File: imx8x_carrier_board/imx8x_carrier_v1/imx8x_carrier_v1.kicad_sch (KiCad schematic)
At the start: 0 parts

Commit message: Schematic Updates
WIP
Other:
- note added: "JTAG-Misc..................................................Page 10"
- note removed: "GPIO-JTAG-Misc........................................Page 10"
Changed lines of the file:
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@@
 		)
 	)
-	(text "GPIO-JTAG-Misc........................................Page 10\n"
+	(text "JTAG-Misc..................................................Page 10\n"
 		(exclude_from_sim no)
 		(at 46.99 63.5 0)
@@
 			)
 		)
+		(property "Sim.Enable" "0"
+			(at 149.225 37.465 0)
+			(effects
+				(font
+					(size 1.27 1.27)
+				)
+				(hide yes)
+			)
+		)
 		(instances
 			(project "imx8x_carrier_v1"
@@
 			)
 		)
+		(property "Sim.Enable" "0"
+			(at 126.365 50.165 0)
+			(effects
+				(font
+					(size 1.27 1.27)
+				)
+				(hide yes)
+			)
+		)
 		(instances
 			(project "imx8x_carrier_v1"
@@
 			)
 		)
+		(property "Sim.Enable" "0"
+			(at 126.365 45.72 0)
+			(effects
+				(font
+					(size 1.27 1.27)
+				)
+				(hide yes)
+			)
+		)
 		(instances
 			(project "imx8x_carrier_v1"
@@
 			)
 		)
+		(property "Sim.Enable" "0"
+			(at 149.225 59.69 0)
+			(effects
+				(font
+					(size 1.27 1.27)
+				)
+				(hide yes)
+			)
+		)
 		(instances
 			(project "imx8x_carrier_v1"
@@
 			)
 		)
+		(property "Sim.Enable" "0"
+			(at 160.655 33.02 0)
+			(effects
+				(font
+					(size 1.27 1.27)
+				)
+				(hide yes)
+			)
+		)
 		(instances
 			(project "imx8x_carrier_v1"
@@
 			)
 		)
+		(property "Sim.Enable" "0"
+			(at 160.655 85.725 0)
+			(effects
+				(font
+					(size 1.27 1.27)
+				)
+				(hide yes)
+			)
+		)
 		(instances
 			(project "imx8x_carrier_v1"
@@
 			)
 		)
+		(property "Sim.Enable" "0"
+			(at 173.355 58.42 0)
+			(effects
+				(font
+					(size 1.27 1.27)
+				)
+				(hide yes)
+			)
+		)
 		(instances
 			(project "imx8x_carrier_v1"
@@
 			)
 		)
+		(property "Sim.Enable" "0"
+			(at 119.38 89.535 0)
+			(effects
+				(font
+					(size 1.27 1.27)
+				)
+				(hide yes)
+			)
+		)
 		(instances
 			(project ""
@@
 			)
 		)
+		(property "Sim.Enable" "0"
+			(at 137.795 27.305 0)
+			(effects
+				(font
+					(size 1.27 1.27)
+				)
+				(hide yes)
+			)
+		)
 		(instances
 			(project "imx8x_carrier_v1"
@@
 			)
 		)
+		(property "Sim.Enable" "0"
+			(at 149.225 67.945 0)
+			(effects
+				(font
+					(size 1.27 1.27)
+				)
+				(hide yes)
+			)
+		)
 		(instances
 			(project "imx8x_carrier_v1"
@@
 			)
 		)
+		(property "Sim.Enable" "0"
+			(at 149.225 48.26 0)
+			(effects
+				(font
+					(size 1.27 1.27)
+				)
+				(hide yes)
+			)
+		)
 		(instances
 			(project "imx8x_carrier_v1"
@@
 			(at 149.225 78.74 0)
 			(effects
+				(font
+					(size 1.27 1.27)
+				)
+				(hide yes)
+			)
+		)
+		(property "Sim.Enable" "0"
+			(at 149.225 78.74 0)
+			(effects

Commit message: Schematic Updates
WIP
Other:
- sheet GPIO - JTAG - Misc. renamed JTAG - Misc. (page 10)

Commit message: Update to Schematic
Did some overview of the schematic and did some touch ups. There are still some GPIOs that need to wired to pins.
All signals should be named correctly and connected the same.

Will need a document review before PCB layout.
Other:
- note added: "Need to put in all the GPIO remaining pins"
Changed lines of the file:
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@@
+		)
+	)
+	(text "Need to put in all the GPIO remaining pins"
+		(exclude_from_sim no)
+		(at 40.64 85.725 0)
+		(effects
+			(font
+				(size 1.27 1.27)
+			)
 		)
 	)
@@
 		(at 147.955 41.91 0)
 		(unit 1)
-		(exclude_from_sim yes)
+		(exclude_from_sim no)
 		(in_bom no)
 		(on_board no)
@@
 		(at 125.095 54.61 0)
 		(unit 1)
-		(exclude_from_sim yes)
+		(exclude_from_sim no)
 		(in_bom no)
 		(on_board no)
@@
 		(at 125.095 50.165 0)
 		(unit 1)
-		(exclude_from_sim yes)
+		(exclude_from_sim no)
 		(in_bom no)
 		(on_board no)
@@
 		(at 147.955 64.135 0)
 		(unit 1)
-		(exclude_from_sim yes)
+		(exclude_from_sim no)
 		(in_bom no)
 		(on_board no)
@@
 		(at 159.385 37.465 270)
 		(unit 1)
-		(exclude_from_sim yes)
+		(exclude_from_sim no)
 		(in_bom no)
 		(on_board no)
@@
 		(at 159.385 90.17 90)
 		(unit 1)
-		(exclude_from_sim yes)
+		(exclude_from_sim no)
 		(in_bom no)
 		(on_board no)
@@
 		(at 172.085 62.865 0)
 		(unit 1)
-		(exclude_from_sim yes)
+		(exclude_from_sim no)
 		(in_bom no)
 		(on_board no)
@@
 		(at 118.11 93.98 0)
 		(unit 1)
-		(exclude_from_sim yes)
+		(exclude_from_sim no)
 		(in_bom no)
 		(on_board no)
@@
 		(at 136.525 31.75 0)
 		(unit 1)
-		(exclude_from_sim yes)
+		(exclude_from_sim no)
 		(in_bom no)
 		(on_board no)
@@
 		(at 147.955 72.39 0)
 		(unit 1)
-		(exclude_from_sim yes)
+		(exclude_from_sim no)
 		(in_bom no)
 		(on_board no)
@@
 		(at 147.955 52.705 0)
 		(unit 1)
-		(exclude_from_sim yes)
+		(exclude_from_sim no)
 		(in_bom no)
 		(on_board no)
@@
 		(at 147.955 83.185 0)
 		(unit 1)
-		(exclude_from_sim yes)
-		(in_bom no)
-		(on_board no)
+		(exclude_from_sim no)
+		(in_bom no)
+		(on_board no)

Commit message: WIP
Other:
- sheet JTAG - Misc. (page 10) renamed JTAG - Misc.
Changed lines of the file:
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@@
 			(color 255 223 38 1.0000)
 		)
-		(property "Sheetname" "JTAG - Misc. (page 10)"
+		(property "Sheetname" "JTAG - Misc."
 			(at 127.635 80.5684 0)
 			(effects

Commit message: Schematic Complete
The IMX8X Scales carrier board is done being finalized. Cleaned up lots of things. This updated schematic should be ready for a full layout and track routing process. Only ERC errors are pin types which we dont really care about. All capacitor voltages have been reincluded since they were cleared by a kicad bug.
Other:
- note removed: "Need to put in all the GPIO remaining pins"
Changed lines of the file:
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@@
-		)
-	)
-	(text "Need to put in all the GPIO remaining pins"
-		(exclude_from_sim no)
-		(at 40.64 85.725 0)
-		(effects
-			(font
-				(size 1.27 1.27)
-			)
 		)
 	)
@@
 	)
 	(symbol
-		(lib_id "Graphic:SYM_Arrow_Normal")
+		(lib_id "imx8_carrier_board_symbol_library:SYM_Arrow_Normal")
 		(at 147.955 41.91 0)
 		(unit 1)
 		(exclude_from_sim no)
 		(in_bom no)
-		(on_board no)
+		(on_board yes)
 		(dnp no)
 		(fields_autoplaced yes)
@@
 		)
 		(property "Description" "Filled arrow, 200mil"
+			(at 147.955 41.91 0)
+			(effects
+				(font
+					(size 1.27 1.27)
+				)
+				(hide yes)
+			)
+		)
+		(property "Sim.Enable" "0"
 			(at 147.955 41.91 0)
 			(effects
@@
 	)
 	(symbol
-		(lib_id "Graphic:SYM_Arrow_Normal")
+		(lib_id "imx8_carrier_board_symbol_library:SYM_Arrow_Normal")
 		(at 125.095 54.61 0)
 		(unit 1)
 		(exclude_from_sim no)
 		(in_bom no)
-		(on_board no)
+		(on_board yes)
 		(dnp no)
 		(fields_autoplaced yes)
@@
 		)
 		(property "Description" "Filled arrow, 200mil"
+			(at 125.095 54.61 0)
+			(effects
+				(font
+					(size 1.27 1.27)
+				)
+				(hide yes)
+			)
+		)
+		(property "Sim.Enable" "0"
 			(at 125.095 54.61 0)
 			(effects
@@
 	)
 	(symbol
-		(lib_id "Graphic:SYM_Arrow_Normal")
+		(lib_id "imx8_carrier_board_symbol_library:SYM_Arrow_Normal")
 		(at 125.095 50.165 0)
 		(unit 1)
 		(exclude_from_sim no)
 		(in_bom no)
-		(on_board no)
+		(on_board yes)
 		(dnp no)
 		(fields_autoplaced yes)
@@
 		)
 		(property "Description" "Filled arrow, 200mil"
+			(at 125.095 50.165 0)
+			(effects
+				(font
+					(size 1.27 1.27)
+				)
+				(hide yes)
+			)
+		)
+		(property "Sim.Enable" "0"
 			(at 125.095 50.165 0)
 			(effects
@@
 	)
 	(symbol
-		(lib_id "Graphic:SYM_Arrow_Normal")
+		(lib_id "imx8_carrier_board_symbol_library:SYM_Arrow_Normal")
 		(at 147.955 64.135 0)
 		(unit 1)
 		(exclude_from_sim no)
 		(in_bom no)
-		(on_board no)
+		(on_board yes)
 		(dnp no)
 		(fields_autoplaced yes)
@@
 		)
 		(property "Description" "Filled arrow, 200mil"
+			(at 147.955 64.135 0)
+			(effects
+				(font
+					(size 1.27 1.27)
+				)
+				(hide yes)
+			)
+		)
+		(property "Sim.Enable" "0"
 			(at 147.955 64.135 0)
 			(effects
@@
 	)
 	(symbol
-		(lib_id "Graphic:SYM_Arrow_Normal")
+		(lib_id "imx8_carrier_board_symbol_library:SYM_Arrow_Normal")
 		(at 159.385 37.465 270)
 		(unit 1)
 		(exclude_from_sim no)
 		(in_bom no)
-		(on_board no)
+		(on_board yes)
 		(dnp no)
 		(fields_autoplaced yes)
@@
 		)
 		(property "Description" "Filled arrow, 200mil"
+			(at 159.385 37.465 0)
+			(effects
+				(font
+					(size 1.27 1.27)
+				)
+				(hide yes)
+			)
+		)
+		(property "Sim.Enable" "0"
 			(at 159.385 37.465 0)
 			(effects
@@
 	)
 	(symbol
-		(lib_id "Graphic:SYM_Arrow_Normal")
+		(lib_id "imx8_carrier_board_symbol_library:SYM_Arrow_Normal")
 		(at 159.385 90.17 90)
 		(unit 1)
 		(exclude_from_sim no)
 		(in_bom no)
-		(on_board no)
+		(on_board yes)
 		(dnp no)
 		(fields_autoplaced yes)
@@
 		)
 		(property "Description" "Filled arrow, 200mil"
+			(at 159.385 90.17 0)
+			(effects
+				(font
+					(size 1.27 1.27)
+				)
+				(hide yes)
+			)
+		)
+		(property "Sim.Enable" "0"
 			(at 159.385 90.17 0)
 			(effects
@@
 	)
 	(symbol
-		(lib_id "Graphic:SYM_Arrow_Normal")
+		(lib_id "imx8_carrier_board_symbol_library:SYM_Arrow_Normal")
 		(at 172.085 62.865 0)
 		(unit 1)
 		(exclude_from_sim no)
 		(in_bom no)
-		(on_board no)
+		(on_board yes)
 		(dnp no)
 		(fields_autoplaced yes)
@@
 		)
 		(property "Description" "Filled arrow, 200mil"
+			(at 172.085 62.865 0)
+			(effects
+				(font
+					(size 1.27 1.27)
+				)
+				(hide yes)
+			)
+		)
+		(property "Sim.Enable" "0"
 			(at 172.085 62.865 0)
 			(effects
@@
 	)
 	(symbol
-		(lib_id "Graphic:SYM_Arrow_Normal")
+		(lib_id "imx8_carrier_board_symbol_library:SYM_Arrow_Normal")
 		(at 118.11 93.98 0)
 		(unit 1)
 		(exclude_from_sim no)
 		(in_bom no)
-		(on_board no)
+		(on_board yes)
 		(dnp no)
 		(fields_autoplaced yes)
@@
 		)
 		(property "Description" "Filled arrow, 200mil"
+			(at 118.11 93.98 0)
+			(effects
+				(font
+					(size 1.27 1.27)
+				)
+				(hide yes)
+			)
+		)
+		(property "Sim.Enable" "0"
 			(at 118.11 93.98 0)
 			(effects
@@
 	)
 	(symbol
-		(lib_id "Graphic:SYM_Arrow_Normal")
+		(lib_id "imx8_carrier_board_symbol_library:SYM_Arrow_Normal")
 		(at 136.525 31.75 0)
 		(unit 1)
 		(exclude_from_sim no)
 		(in_bom no)
-		(on_board no)
+		(on_board yes)
 		(dnp no)
 		(fields_autoplaced yes)
@@
 		)
 		(property "Description" "Filled arrow, 200mil"
+			(at 136.525 31.75 0)
+			(effects
+				(font
+					(size 1.27 1.27)
+				)
+				(hide yes)
+			)
+		)
+		(property "Sim.Enable" "0"
 			(at 136.525 31.75 0)
 			(effects
@@
 	)
 	(symbol
-		(lib_id "Graphic:SYM_Arrow_Normal")
+		(lib_id "imx8_carrier_board_symbol_library:SYM_Arrow_Normal")
 		(at 147.955 72.39 0)
 		(unit 1)
 		(exclude_from_sim no)
 		(in_bom no)
-		(on_board no)
+		(on_board yes)
 		(dnp no)
 		(fields_autoplaced yes)
@@
 		)
 		(property "Description" "Filled arrow, 200mil"
+			(at 147.955 72.39 0)
+			(effects
+				(font
+					(size 1.27 1.27)
+				)
+				(hide yes)
+			)
+		)
+		(property "Sim.Enable" "0"
 			(at 147.955 72.39 0)
 			(effects
@@
 	)
 	(symbol
-		(lib_id "Graphic:SYM_Arrow_Normal")
+		(lib_id "imx8_carrier_board_symbol_library:SYM_Arrow_Normal")
 		(at 147.955 52.705 0)
 		(unit 1)
 		(exclude_from_sim no)
 		(in_bom no)
-		(on_board no)
+		(on_board yes)
 		(dnp no)
 		(fields_autoplaced yes)
@@
 		)
 		(property "Description" "Filled arrow, 200mil"
+			(at 147.955 52.705 0)
+			(effects
+				(font
+					(size 1.27 1.27)
+				)
+				(hide yes)
+			)
+		)
+		(property "Sim.Enable" "0"
 			(at 147.955 52.705 0)
 			(effects
@@
 	)
 	(symbol
-		(lib_id "Graphic:SYM_Arrow_Normal")
+		(lib_id "imx8_carrier_board_symbol_library:SYM_Arrow_Normal")
 		(at 147.955 83.185 0)
 		(unit 1)
 		(exclude_from_sim no)
 		(in_bom no)
-		(on_board no)
+		(on_board yes)
 		(dnp no)
 		(fields_autoplaced yes)
@@
 			(at 147.955 83.185 0)
 			(effects
+				(font
+					(size 1.27 1.27)
+				)
+				(hide yes)
+			)
+		)
+		(property "Sim.Enable" "0"
+			(at 147.955 83.185 0)
+			(effects

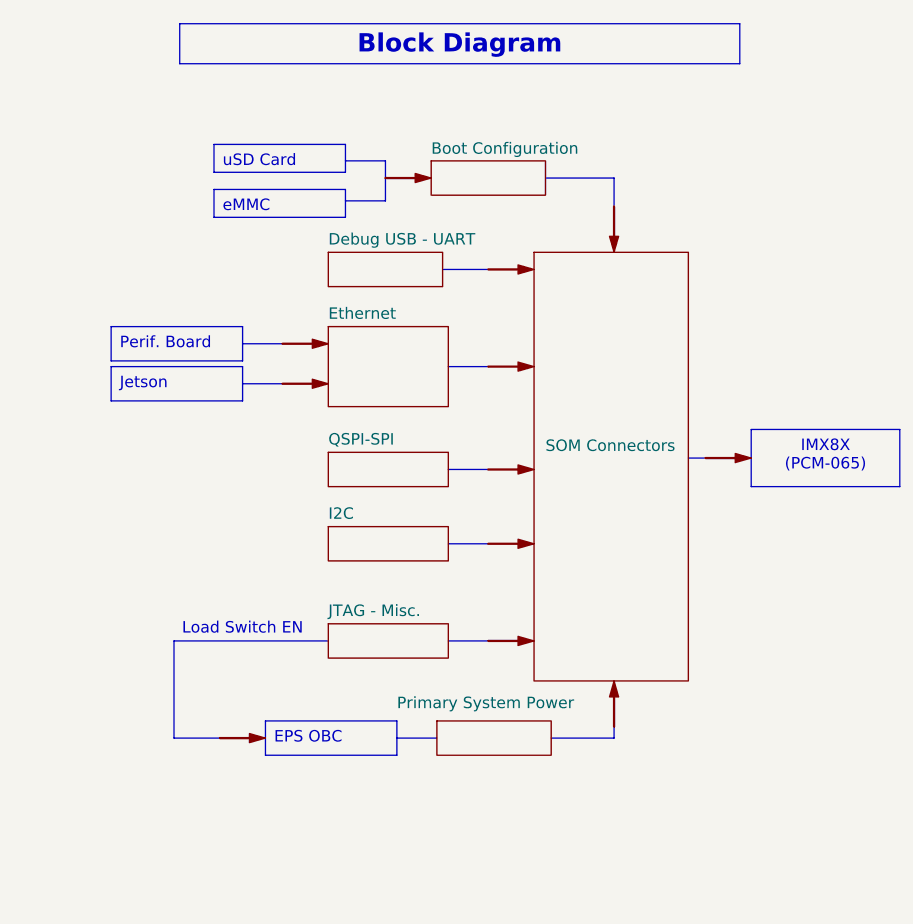
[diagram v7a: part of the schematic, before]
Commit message: Minor Schematic Changes. OK OK its technically done. Time for Layout
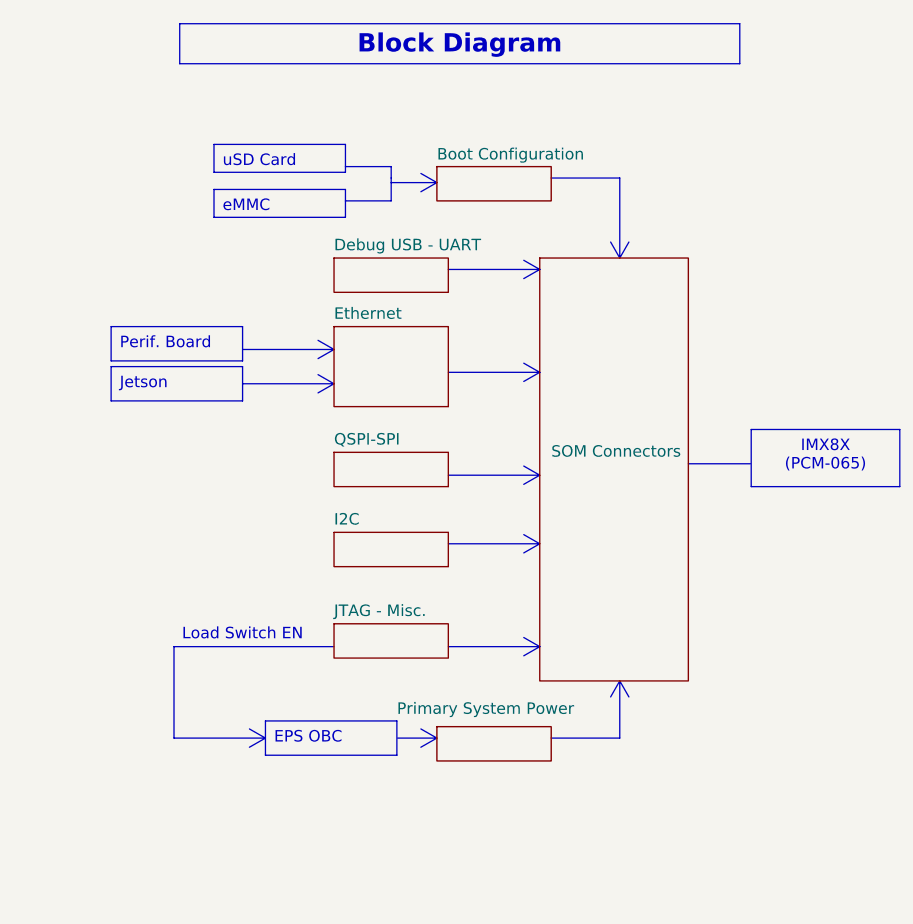
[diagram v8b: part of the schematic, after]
